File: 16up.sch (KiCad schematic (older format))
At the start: 20 parts, among them CN1 EXPANSION_PORT, CN2 ALMOST_USERPORT, CN3 CONN_UPORT254, CN4 TAPE_IN, U1 GAL20V8, U102 74LS654, U2 MOS_6529, U3 MOS_6551_ACIA, U4 74HCT04, Y1 1.8432M

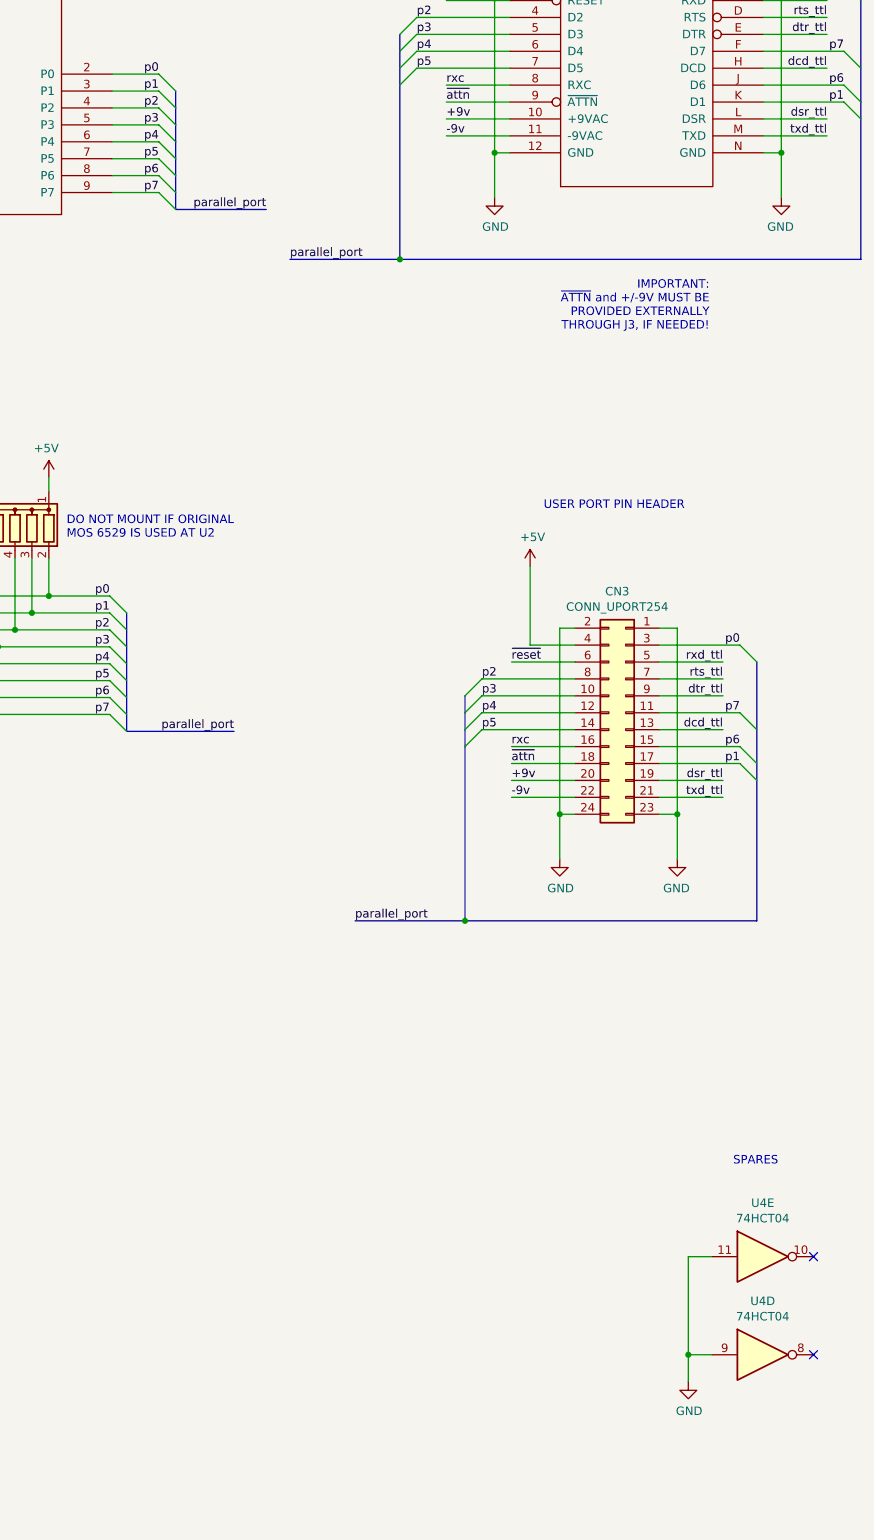
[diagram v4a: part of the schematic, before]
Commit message: Add optional buffering for TX
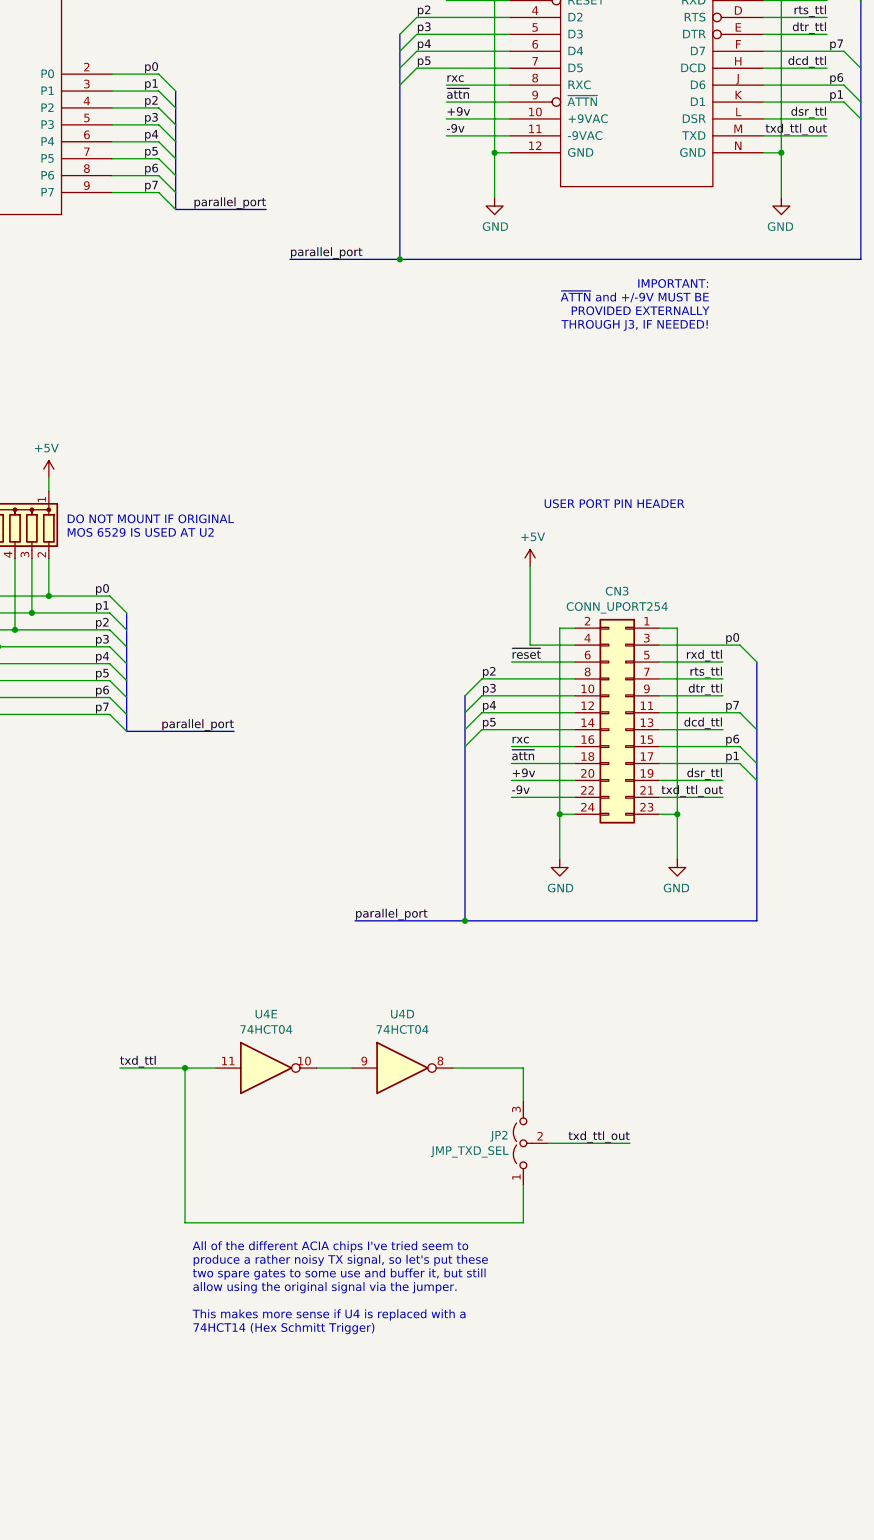
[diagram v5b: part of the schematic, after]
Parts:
- added JP2: JMP_TXD_SEL, Jumper:SolderJumper-3_P1.3mm_Open_RoundedPad1.0x1.5mm, symbol Jumper:Jumper_3_Open
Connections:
- net GND: no longer U4.11, U4.9
- net txd_ttl: now also U4.11, JP2.1 (A); no longer CN2.M (TXD), CN3.21 (Pin_21)
- net at U4.8: now also JP2.3 (B)
- net at U4.10: now also U4.9
- new net txd_ttl_out: CN2.M (TXD), CN3.21 (Pin_21), JP2.2 (C)
- no-connect marks 25 -> 23
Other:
- note added: "All of the different ACIA chips I've tried seem to\nproduce a rather noisy TX signal, so let's put these\ntwo spare gates to some use and buffer it, but still\nallow using the original signal via the jumper.\n\nThis makes more sense if U4 is replaced with a\n74HCT14 (Hex Schmitt Trigger)"
- note removed: "SPARES"
- moved on the sheet: U4D, U4E
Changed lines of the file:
@@
 Sheet 1 1
 Title "16up"
-Date "2024-03-24"
+Date "2024-09-07"
 Rev "3git"
 Comp "SukkoPera & The Folks From The Plus/4 World Forum"
@@
 L 74xx:74HCT04 U4
 U 4 1 641A935F
-P 15300 9465
-F 0 "U4" H 15300 9782 50  0000 C CNN
-F 1 "74HCT04" H 15300 9691 50  0000 C CNN
-F 2 "Package_DIP:DIP-14_W7.62mm_Socket_LongPads" H 15300 9465 50  0001 C CNN
-F 3 "https://assets.nexperia.com/documents/data-sheet/74HC_HCT04.pdf" H 15300 9465 50  0001 C CNN
-	4    15300 9465
+P 13170 7770
+F 0 "U4" H 13170 8087 50  0000 C CNN
+F 1 "74HCT04" H 13170 7996 50  0000 C CNN
+F 2 "Package_DIP:DIP-14_W7.62mm_Socket_LongPads" H 13170 7770 50  0001 C CNN
+F 3 "https://assets.nexperia.com/documents/data-sheet/74HC_HCT04.pdf" H 13170 7770 50  0001 C CNN
+	4    13170 7770
 	1    0    0    -1
 $EndComp
@@
 L 74xx:74HCT04 U4
 U 5 1 641AA758
-P 15300 8885
-F 0 "U4" H 15300 9202 50  0000 C CNN
-F 1 "74HCT04" H 15300 9111 50  0000 C CNN
-F 2 "Package_DIP:DIP-14_W7.62mm_Socket_LongPads" H 15300 8885 50  0001 C CNN
-F 3 "https://assets.nexperia.com/documents/data-sheet/74HC_HCT04.pdf" H 15300 8885 50  0001 C CNN
-	5    15300 8885
+P 12365 7770
+F 0 "U4" H 12365 8087 50  0000 C CNN
+F 1 "74HCT04" H 12365 7996 50  0000 C CNN
+F 2 "Package_DIP:DIP-14_W7.62mm_Socket_LongPads" H 12365 7770 50  0001 C CNN
+F 3 "https://assets.nexperia.com/documents/data-sheet/74HC_HCT04.pdf" H 12365 7770 50  0001 C CNN
+	5    12365 7770
 	1    0    0    -1
 $EndComp
@@
 	1    0    0    -1
 $EndComp
-NoConn ~ 15600 8885
-Text Notes 15125 8350 0    50   ~ 0
-SPARES
 Text Label 10410 8320 2    50   ~ 0
 dsr_ttl
@@
 dsr_ttl
 Text Label 15680 2260 2    50   ~ 0
-txd_ttl
+txd_ttl_out
 Wire Wire Line
 	4230 6090 3485 6090
@@
 dsr_ttl
 Text Label 15065 6170 2    50   ~ 0
-txd_ttl
+txd_ttl_out
 Text Label 13430 2060 0    50   ~ 0
 ~attn
@@
 Wire Wire Line
 	13805 2060 13430 2060
-NoConn ~ 15600 9465
-Wire Wire Line
-	15000 8885 14860 8885
-Wire Wire Line
-	14860 8885 14860 9465
-Wire Wire Line
-	15000 9465 14860 9465
-Connection ~ 14860 9465
-Wire Wire Line
-	14860 9465 14860 9625
-$Comp
-L power:GND #PWR0116
-U 1 1 6455627D
-P 14860 9625
-F 0 "#PWR0116" H 14860 9375 50  0001 C CNN
-F 1 "GND" H 14865 9452 50  0000 C CNN
-F 2 "" H 14860 9625 50  0001 C CNN
-F 3 "" H 14860 9625 50  0001 C CNN
-	1    14860 9625
-	1    0    0    -1
-$EndComp
 $Comp
 L 74LS652:74LS652 U102
@@
 Text Notes 9250 4025 0    50   ~ 0
 MOS 6529 REPLACEMENT CIRCUIT\nBY DANIEL MANTIONE\n(ALTERNATIVE TO U2)
-Wire Bus Line
-	15265 5370 15265 6900
-Wire Bus Line
-	13540 5570 13540 6900
-Wire Bus Line
-	15880 1460 15880 2990
-Wire Bus Line
-	13155 1660 13155 2990
-Wire Bus Line
-	9580 1995 9580 2695
-Wire Bus Line
-	1310 3005 1310 3705
-Wire Bus Line
-	6105 6090 6105 6790
-Wire Bus Line
-	11830 1995 11830 2695
-Wire Bus Line
-	11540 5080 11540 5780
-Wire Bus Line
-	7855 5180 7855 5880
-Wire Bus Line
-	3630 2205 3630 3705
-Wire Bus Line
-	5500 1470 5500 2575
 $Comp
 L Logic_Programmable:PAL20L8 U1
@@
 	1    0    0    -1
 $EndComp
+Wire Wire Line
+	12665 7770 12870 7770
+Wire Wire Line
+	11500 7770 11885 7770
+Text Label 14515 8215 2    50   ~ 0
+txd_ttl_out
+$Comp
+L Jumper:Jumper_3_Open JP2
+U 1 1 66E8EB05
+P 13885 8215
+F 0 "JP2" V 13931 8302 50  0000 L CNN
+F 1 "JMP_TXD_SEL" V 13840 8302 50  0000 L CNN
+F 2 "Jumper:SolderJumper-3_P1.3mm_Open_RoundedPad1.0x1.5mm" H 13885 8215 50  0001 C CNN
+F 3 "~" H 13885 8215 50  0001 C CNN
+	1    13885 8215
+	0    -1   -1   0
+$EndComp
+Wire Wire Line
+	14035 8215 14515 8215
+Wire Wire Line
+	13885 7965 13885 7770
+Wire Wire Line
+	13470 7770 13885 7770
+Wire Wire Line
+	13885 8465 13885 8685
+Wire Wire Line
+	13885 8685 11885 8685
+Wire Wire Line
+	11885 8685 11885 7770
+Connection ~ 11885 7770
+Wire Wire Line
+	11885 7770 12065 7770
+Text Notes 11930 9345 0    50   ~ 0
+All of the different ACIA chips I've tried seem to\nproduce a rather noisy TX signal, so let's put these\ntwo spare gates to some use and buffer it, but still\nallow using the original signal via the jumper.\n\nThis makes more sense if U4 is replaced with a\n74HCT14 (Hex Schmitt Trigger)
+Wire Bus Line
+	15265 5370 15265 6900
+Wire Bus Line
+	13540 5570 13540 6900
+Wire Bus Line
+	15880 1460 15880 2990
+Wire Bus Line
+	13155 1660 13155 2990
+Wire Bus Line
+	9580 1995 9580 2695
+Wire Bus Line
+	1310 3005 1310 3705
+Wire Bus Line
+	6105 6090 6105 6790
+Wire Bus Line
+	11830 1995 11830 2695
+Wire Bus Line
+	11540 5080 11540 5780
+Wire Bus Line
+	7855 5180 7855 5880
+Wire Bus Line
+	3630 2205 3630 3705
+Wire Bus Line
+	5500 1470 5500 2575
+Text Label 11500 7770 0    50   ~ 0
+txd_ttl
 $EndSCHEMATC
